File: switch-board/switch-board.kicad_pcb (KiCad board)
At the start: 2 copper layers, 38.1 x 38.1 mm, 22 parts, among them J1 VIN, J2 CTRL, J3 RF_XOUT, J4 RF_XIN, J5 RF_YIN, J6 RF_YOUT, J7 GND, K1 G2RL-1-E, Q1 BS170F

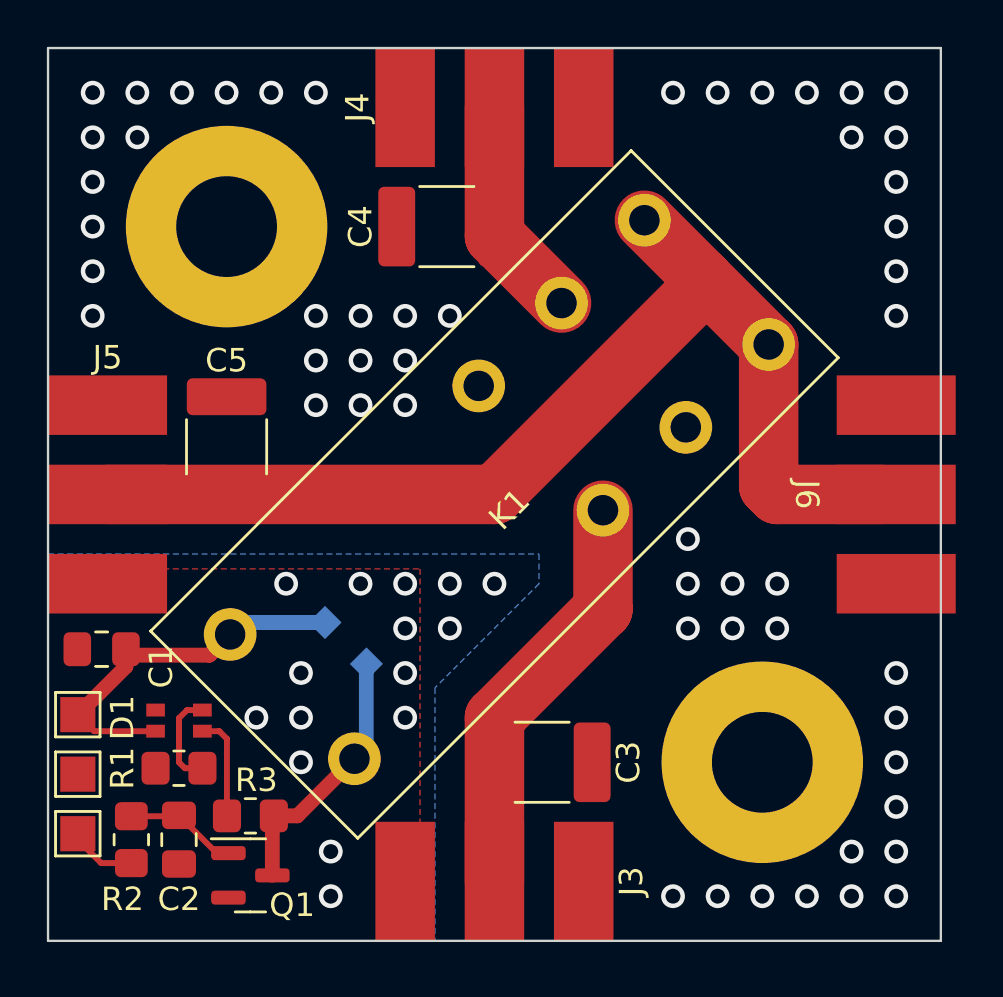
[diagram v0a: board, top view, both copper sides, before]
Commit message: finalized single-point switch design, more work on 4x4 matrix
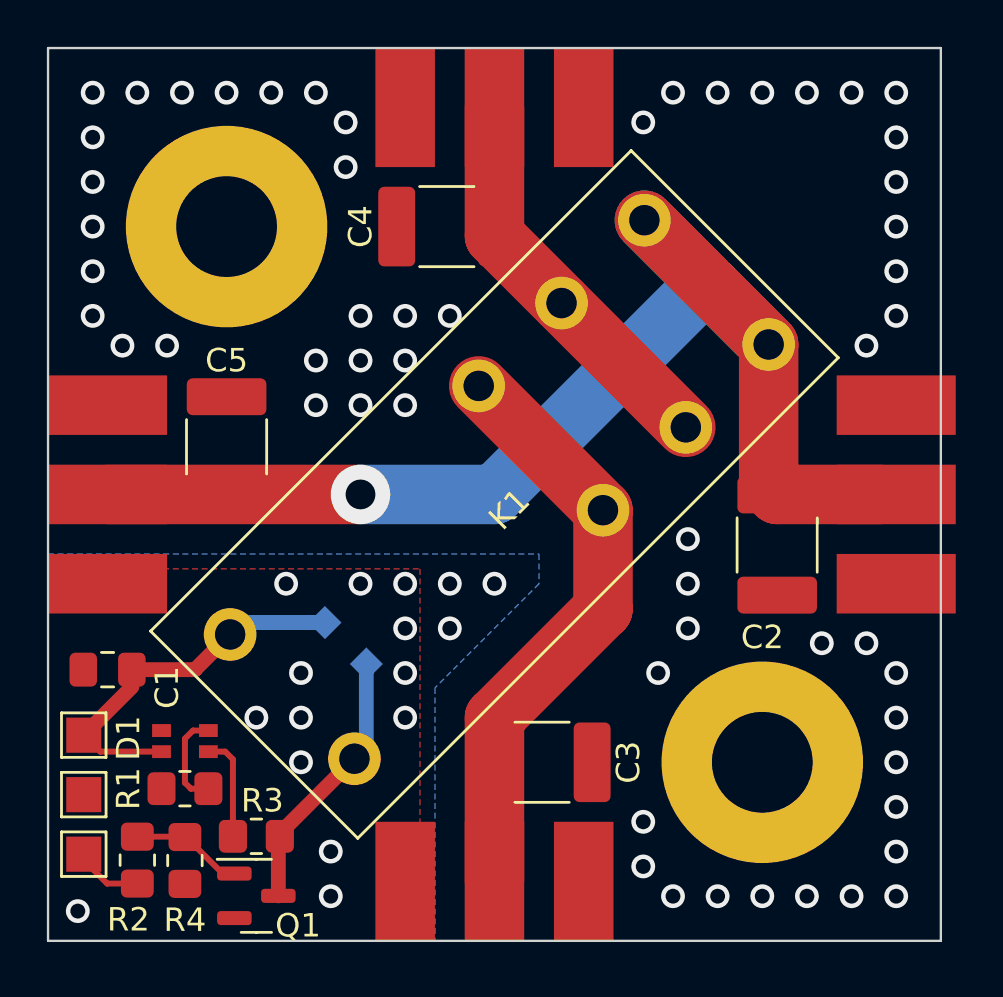
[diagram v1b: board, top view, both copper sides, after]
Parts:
- added R4: 10k, Resistor_SMD:R_0805_2012Metric_Pad1.20x1.40mm_HandSolder, F.Cu at (94.7, 79.1)
- C2: value 0.1uF -> NP; footprint Capacitor_SMD:C_0805_2012Metric_Pad1.18x1.45mm_HandSolder -> Capacitor_SMD:C_1812_4532Metric_Pad1.57x3.40mm_HandSolder
- moved C2 28.5 mm to (120.0, 65.7), turned to 90 degrees
- moved G*** 1.08 mm to (121.4, 50.0)
- moved D1 0.91 mm to (94.7, 74.0)
- moved J1 0.91 mm to (90.4, 73.8)
- moved J2 0.91 mm to (90.4, 78.9)
- moved J7 0.91 mm to (90.4, 76.3)
- moved Q1 0.91 mm to (97.8, 80.6)
- moved R1 0.91 mm to (94.7, 76.1)
- moved R3 0.91 mm to (97.8, 78.1)
- moved C1 0.91 mm to (91.4, 71.0)
- moved R2 0.91 mm to (92.7, 79.1)
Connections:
- C2 pad 1: Net-(C2-Pad1) -> GND
- C2 pad 2: GND -> Net-(J6-Pad1)
- C5 pad 2: Net-(C5-Pad2) -> Net-(J6-Pad1)
- J5 pad 1: Net-(C5-Pad2) -> Net-(J6-Pad1)
- J6 pad 1: Net-(C5-Pad2) -> Net-(J6-Pad1)
- K1 pad 4: Net-(C5-Pad2) -> Net-(J6-Pad1)
- Q1 pad 1: Net-(C2-Pad1) -> Net-(Q1-Pad1)
- R2 pad 2: Net-(C2-Pad1) -> Net-(Q1-Pad1)
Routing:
- net Net-(J6-Pad1): track 0.00 -> 55.3 mm, vias 0 -> 1
- net Net-(C5-Pad2): track 47.9 -> 0.00 mm
- net Net-(C4-Pad2): track 9.53 -> 17.0 mm
- net Net-(C3-Pad2): track 17.8 -> 25.3 mm
- net Net-(Q1-Pad1): track 0.00 -> 4.83 mm
- net Net-(C2-Pad1): track 4.83 -> 0.00 mm
- net Net-(C1-Pad2): track 16.3 -> 15.6 mm
- net GND: vias 67 -> 72
- net (no net): vias 1 -> 0
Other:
- board text added: "A 38/22"
